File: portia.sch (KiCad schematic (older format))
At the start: 60 parts, among them J1 USB_B_Micro, J10 Conn_01x02, J11 Conn_01x02, J12 Conn_01x02, J13 Conn_01x02, J14 Conn_01x02, J15 Conn_01x02, J16 Conn_01x04, J3 Conn_01x02, J4 Conn_01x04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

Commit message: ground plane fill
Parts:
- removed D7: LED, LED_SMD:LED_0603_1608Metric, symbol Device:LED
- removed R11: R_Small, Resistor_SMD:R_0603_1608Metric, symbol Device:R_Small
- added D3: LED_ARGB, LED_SMD:LED_RGB_1210, symbol Device:LED_ARGB
- added R11, R18: 75, Resistor_SMD:R_0603_1608Metric, symbol Device:R
- added R19: 100, Resistor_SMD:R_0603_1608Metric, symbol Device:R
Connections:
- net +3V3: now also D3.1 (A)
- net 3.3V: now also U2.5 (VCC); no longer U2.2 (GND)
- net GND: now also U2.2 (GND); no longer U2.5 (VCC)
- net at U4.14 (IO12): now also R11.1
- net at U4.16 (IO13): now also R18.1
- net at U4.26 (IO4): now also R19.1
- new net: D3.2 (RK), R19.2
- new net: D3.3 (GK), R18.2
- new net: D3.4 (BK), R11.2
- no-connect marks 20 -> 25
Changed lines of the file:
@@
-	1    0    0    -1
-$EndComp
-$Comp
-L Connector:USB_B_Micro J1
-U 1 1 5C241362
-P 3450 8650
-F 0 "J1" H 3505 9117 50  0000 C CNN
-F 1 "USB_B_Micro" H 3505 9026 50  0000 C CNN
-F 2 "Connector_USB:USB_Micro-B_Amphenol_10103594-0001LF_Horizontal" H 3600 8600 50  0001 C CNN
-F 3 "~" H 3600 8600 50  0001 C CNN
-	1    3450 8650
 	1    0    0    -1
 $EndComp
@@
 Wire Wire Line
 	3750 8750 4050 8750
-Wire Wire Line
-	3750 8550 3750 8450
-Wire Wire Line
-	3800 9050 3800 9250
-Wire Wire Line
-	3450 9050 3800 9050
 $Comp
 L power:GND #PWR0112
 U 1 1 5C384A73
-P 3800 9250
-F 0 "#PWR0112" H 3800 9000 50  0001 C CNN
-F 1 "GND" H 3805 9077 50  0000 C CNN
-F 2 "" H 3800 9250 50  0001 C CNN
-F 3 "" H 3800 9250 50  0001 C CNN
-	1    3800 9250
+P 3450 9250
+F 0 "#PWR0112" H 3450 9000 50  0001 C CNN
+F 1 "GND" H 3455 9077 50  0000 C CNN
+F 2 "" H 3450 9250 50  0001 C CNN
+F 3 "" H 3450 9250 50  0001 C CNN
+	1    3450 9250
 	1    0    0    -1
 $EndComp
@@
 Wire Wire Line
 	4250 9300 4850 9300
-Wire Wire Line
-	3750 8450 3750 8100
 $Comp
 L power:+5V #PWR0115
@@
 Wire Wire Line
 	3750 8550 3900 8550
-Connection ~ 3750 8450
 Wire Wire Line
 	4100 8550 4500 8550
@@
 Wire Wire Line
 	11000 6250 11200 6250
-Wire Wire Line
-	11200 6250 11200 6700
-$Comp
-L Device:R_Small R11
-U 1 1 5C805139
-P 12300 6700
-F 0 "R11" V 12104 6700 50  0000 C CNN
-F 1 "R_Small" V 12195 6700 50  0000 C CNN
-F 2 "Resistor_SMD:R_0603_1608Metric" H 12300 6700 50  0001 C CNN
-F 3 "~" H 12300 6700 50  0001 C CNN
-	1    12300 6700
-	0    1    1    0
-$EndComp
-Wire Wire Line
-	11200 6700 12200 6700
-Wire Wire Line
-	12400 6700 12650 6700
-$Comp
-L Device:LED D7
-U 1 1 5C853C14
-P 12800 6700
-F 0 "D7" H 12792 6445 50  0000 C CNN
-F 1 "LED" H 12792 6536 50  0000 C CNN
-F 2 "LED_SMD:LED_0603_1608Metric" H 12800 6700 50  0001 C CNN
-F 3 "~" H 12800 6700 50  0001 C CNN
-	1    12800 6700
-	-1   0    0    1
-$EndComp
-Wire Wire Line
-	12950 6700 13200 6700
-$Comp
-L power:GND #PWR0135
-U 1 1 5C8D8953
-P 13200 6700
-F 0 "#PWR0135" H 13200 6450 50  0001 C CNN
-F 1 "GND" V 13205 6572 50  0000 R CNN
-F 2 "" H 13200 6700 50  0001 C CNN
-F 3 "" H 13200 6700 50  0001 C CNN
-	1    13200 6700
-	0    -1   -1   0
-$EndComp
 NoConn ~ 10050 6950
 Text Label 7250 8250 0    50   ~ 0
@@
 Wire Wire Line
 	12300 8650 13500 8650
-Wire Wire Line
-	14700 8250 14800 8250
-Wire Wire Line
-	14700 8650 14850 8650
 $Comp
 L SparkFun-Aesthetics:3.3V #SUPPLY0101
 U 1 1 5C35ADBC
-P 15350 8250
-F 0 "#SUPPLY0101" H 15350 8250 50  0001 L BNN
-F 1 "3.3V" V 15350 8379 50  0000 L CNN
-F 2 "" H 15350 8250 50  0001 C CNN
-F 3 "" H 15350 8250 50  0001 C CNN
-	1    15350 8250
-	0    1    1    0
-$EndComp
-$Comp
-L power:GND #PWR0119
-U 1 1 5C363419
-P 15000 8650
-F 0 "#PWR0119" H 15000 8400 50  0001 C CNN
-F 1 "GND" H 15005 8477 50  0000 C CNN
-F 2 "" H 15000 8650 50  0001 C CNN
-F 3 "" H 15000 8650 50  0001 C CNN
-	1    15000 8650
-	1    0    0    -1
+P 15150 9300
+F 0 "#SUPPLY0101" H 15150 9300 50  0001 L BNN
+F 1 "3.3V" V 15150 9429 50  0000 L CNN
+F 2 "" H 15150 9300 50  0001 C CNN
+F 3 "" H 15150 9300 50  0001 C CNN
+	1    15150 9300
+	0    1    1    0
 $EndComp
 $Comp
@@
 Wire Wire Line
 	13500 7700 13650 7700
-Wire Wire Line
-	14800 7700 14800 8250
 Connection ~ 13650 7700
-Wire Wire Line
-	13650 7700 14800 7700
-Connection ~ 14800 8250
-Wire Wire Line
-	14800 8250 15150 8250
 NoConn ~ 13800 8250
 NoConn ~ 13800 8350
@@
 	13350 9200 13350 8750
 Wire Wire Line
-	14650 9100 14850 9100
-Wire Wire Line
-	14850 9100 14850 8650
-Connection ~ 14850 8650
-Wire Wire Line
-	14850 8650 15000 8650
-Wire Wire Line
 	14650 9300 14800 9300
-Wire Wire Line
-	15150 9300 15150 8250
-Connection ~ 15150 8250
-Wire Wire Line
-	15150 8250 15350 8250
 $Comp
 L Device:R_Small R12
@@
 	1    0    0    -1
 $EndComp
+$Comp
+L Device:LED_ARGB D3
+U 1 1 5C32D160
+P 7950 7350
+F 0 "D3" H 7950 6883 50  0000 C CNN
+F 1 "LED_ARGB" H 7950 6974 50  0000 C CNN
+F 2 "LED_SMD:LED_RGB_1210" H 7950 7300 50  0001 C CNN
+F 3 "~" H 7950 7300 50  0001 C CNN
+	1    7950 7350
+	-1   0    0    1
+$EndComp
+$Comp
+L Device:R R11
+U 1 1 5C36CFF3
+P 8500 7150
+F 0 "R11" V 8400 7050 50  0000 C CNN
+F 1 "75" V 8400 7250 50  0000 C CNN
+F 2 "Resistor_SMD:R_0603_1608Metric" V 8430 7150 50  0001 C CNN
+F 3 "~" H 8500 7150 50  0001 C CNN
+	1    8500 7150
+	0    1    1    0
+$EndComp
+$Comp
+L Device:R R18
+U 1 1 5C36EBA1
+P 8500 7350
+F 0 "R18" V 8400 7250 50  0000 C CNN
+F 1 "75" V 8400 7450 50  0000 C CNN
+F 2 "Resistor_SMD:R_0603_1608Metric" V 8430 7350 50  0001 C CNN
+F 3 "~" H 8500 7350 50  0001 C CNN
+	1    8500 7350
+	0    1    1    0
+$EndComp
+$Comp
+L Device:R R19
+U 1 1 5C36EF8A
+P 8500 7550
+F 0 "R19" V 8400 7450 50  0000 C CNN
+F 1 "100" V 8400 7650 50  0000 C CNN
+F 2 "Resistor_SMD:R_0603_1608Metric" V 8430 7550 50  0001 C CNN
+F 3 "~" H 8500 7550 50  0001 C CNN
+	1    8500 7550
+	0    1    1    0
+$EndComp
+Wire Wire Line
+	9150 6500 8650 6500
+Wire Wire Line
+	8650 6500 8650 7150
+Wire Wire Line
+	8650 7350 9750 7350
+Wire Wire Line
+	9750 7350 9750 6950
+Wire Wire Line
+	11200 6250 11200 6950
+Wire Wire Line
+	10750 6950 10750 7550
+Wire Wire Line
+	10750 7550 8650 7550
+Wire Wire Line
+	11200 6950 10750 6950
+Wire Wire Line
+	8150 7150 8350 7150
+Wire Wire Line
+	8150 7350 8350 7350
+Wire Wire Line
+	8150 7550 8350 7550
+Wire Wire Line
+	7750 7350 7300 7350
+$Comp
+L power:+3.3V #PWR0120
+U 1 1 5C44597A
+P 7300 7350
+F 0 "#PWR0120" H 7300 7200 50  0001 C CNN
+F 1 "+3.3V" V 7315 7478 50  0000 L CNN
+F 2 "" H 7300 7350 50  0001 C CNN
+F 3 "" H 7300 7350 50  0001 C CNN
+	1    7300 7350
+	0    -1   -1   0
+$EndComp
+$Comp
+L power:GND #PWR0119
+U 1 1 5C3312B5
+P 14800 9100
+F 0 "#PWR0119" H 14800 8850 50  0001 C CNN
+F 1 "GND" V 14805 8972 50  0000 R CNN
+F 2 "" H 14800 9100 50  0001 C CNN
+F 3 "" H 14800 9100 50  0001 C CNN
+	1    14800 9100
+	0    -1   -1   0
+$EndComp
+$Comp
+L power:GND #PWR0121
+U 1 1 5C375D80
+P 14800 8250
+F 0 "#PWR0121" H 14800 8000 50  0001 C CNN
+F 1 "GND" H 14805 8077 50  0000 C CNN
+F 2 "" H 14800 8250 50  0001 C CNN
+F 3 "" H 14800 8250 50  0001 C CNN
+	1    14800 8250
+	1    0    0    -1
+$EndComp
+Wire Wire Line
+	14700 8650 15100 8650
+$Comp
+L SparkFun-Aesthetics:3.3V #SUPPLY0102
+U 1 1 5C39E3C3
+P 15150 8650
+F 0 "#SUPPLY0102" H 15150 8650 50  0001 L BNN
+F 1 "3.3V" V 15150 8779 50  0000 L CNN
+F 2 "" H 15150 8650 50  0001 C CNN
+F 3 "" H 15150 8650 50  0001 C CNN
+	1    15150 8650
+	0    1    1    0
+$EndComp
+Wire Wire Line
+	14650 9100 14800 9100
+Wire Wire Line
+	15100 7700 15100 8650
+Wire Wire Line
+	13650 7700 15100 7700
+Connection ~ 15100 8650
+Wire Wire Line
+	15100 8650 15150 8650
+NoConn ~ 13850 9100
+NoConn ~ 12300 8950
+NoConn ~ 12300 9050
+NoConn ~ 12300 9150
+NoConn ~ 12300 9250
+Wire Wire Line
+	3750 8450 3750 8100
+Wire Wire Line
+	3750 8550 3750 8450
+Connection ~ 3750 8450
+$Comp
+L Connector:USB_B_Micro J1
+U 1 1 5C241362
+P 3450 8650
+F 0 "J1" H 3505 9117 50  0000 C CNN
+F 1 "USB_B_Micro" H 3505 9026 50  0000 C CNN
+F 2 "Connector_USB:USB_Micro-B_Amphenol_10103594-0001LF_Horizontal" H 3600 8600 50  0001 C CNN
+F 3 "~" H 3600 8600 50  0001 C CNN
+	1    3450 8650
+	1    0    0    -1
+$EndComp
+Wire Wire Line
+	3450 9050 3450 9250
+Wire Wire Line
+	14700 8250 14800 8250
 $EndSCHEMATC

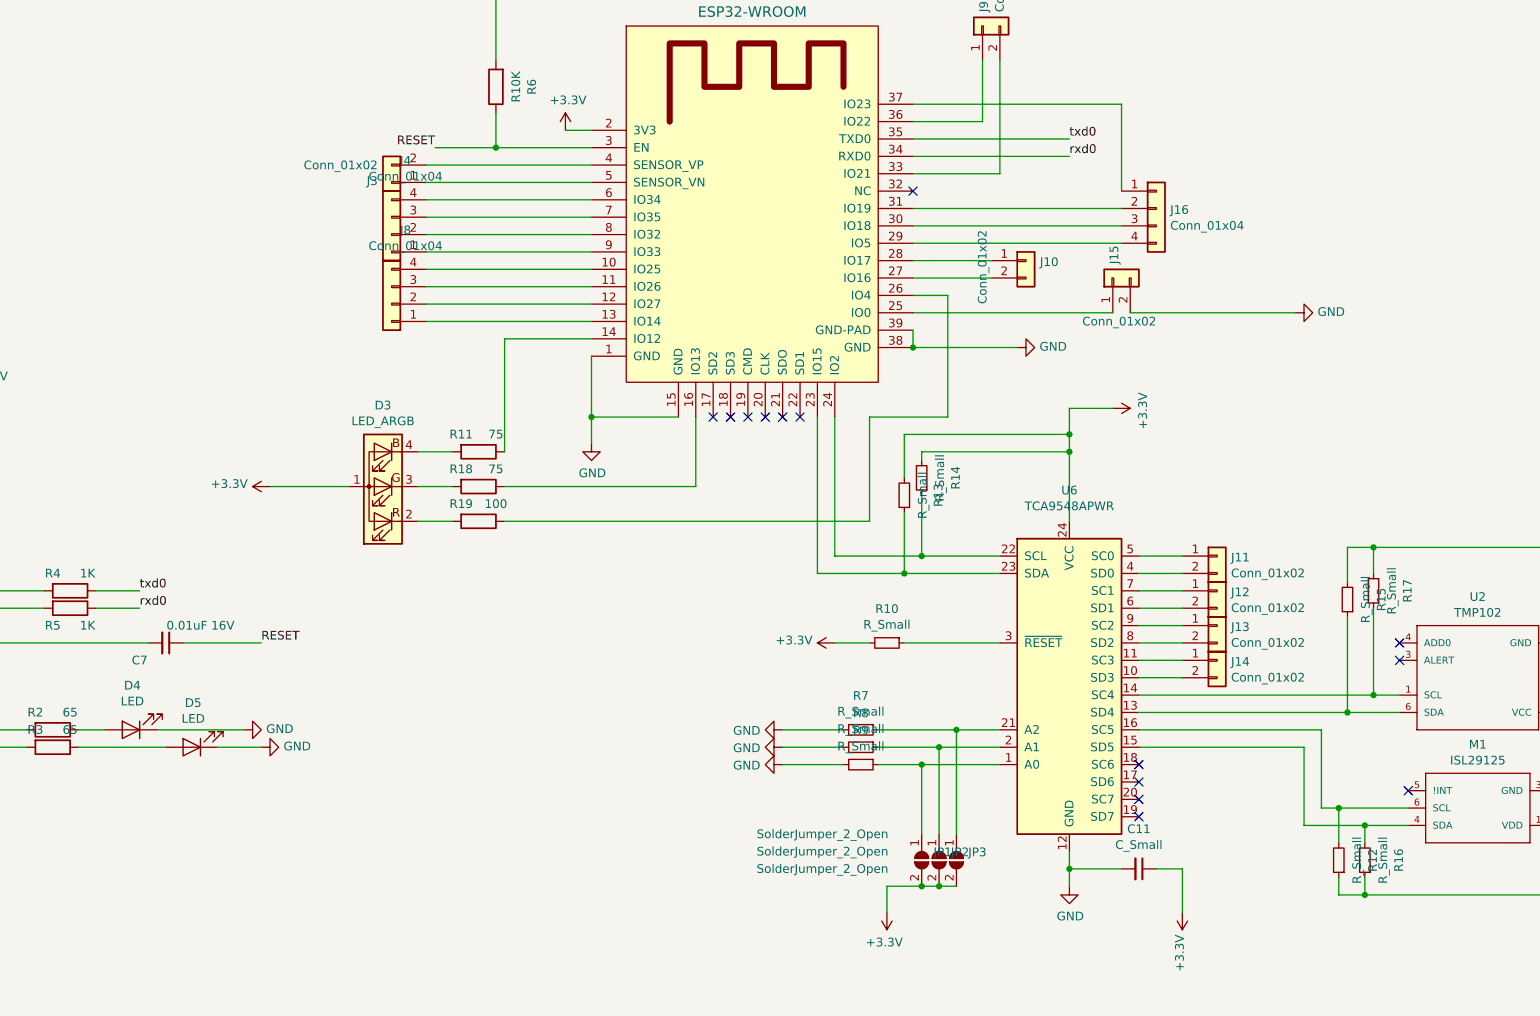
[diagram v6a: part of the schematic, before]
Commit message: added ground ports
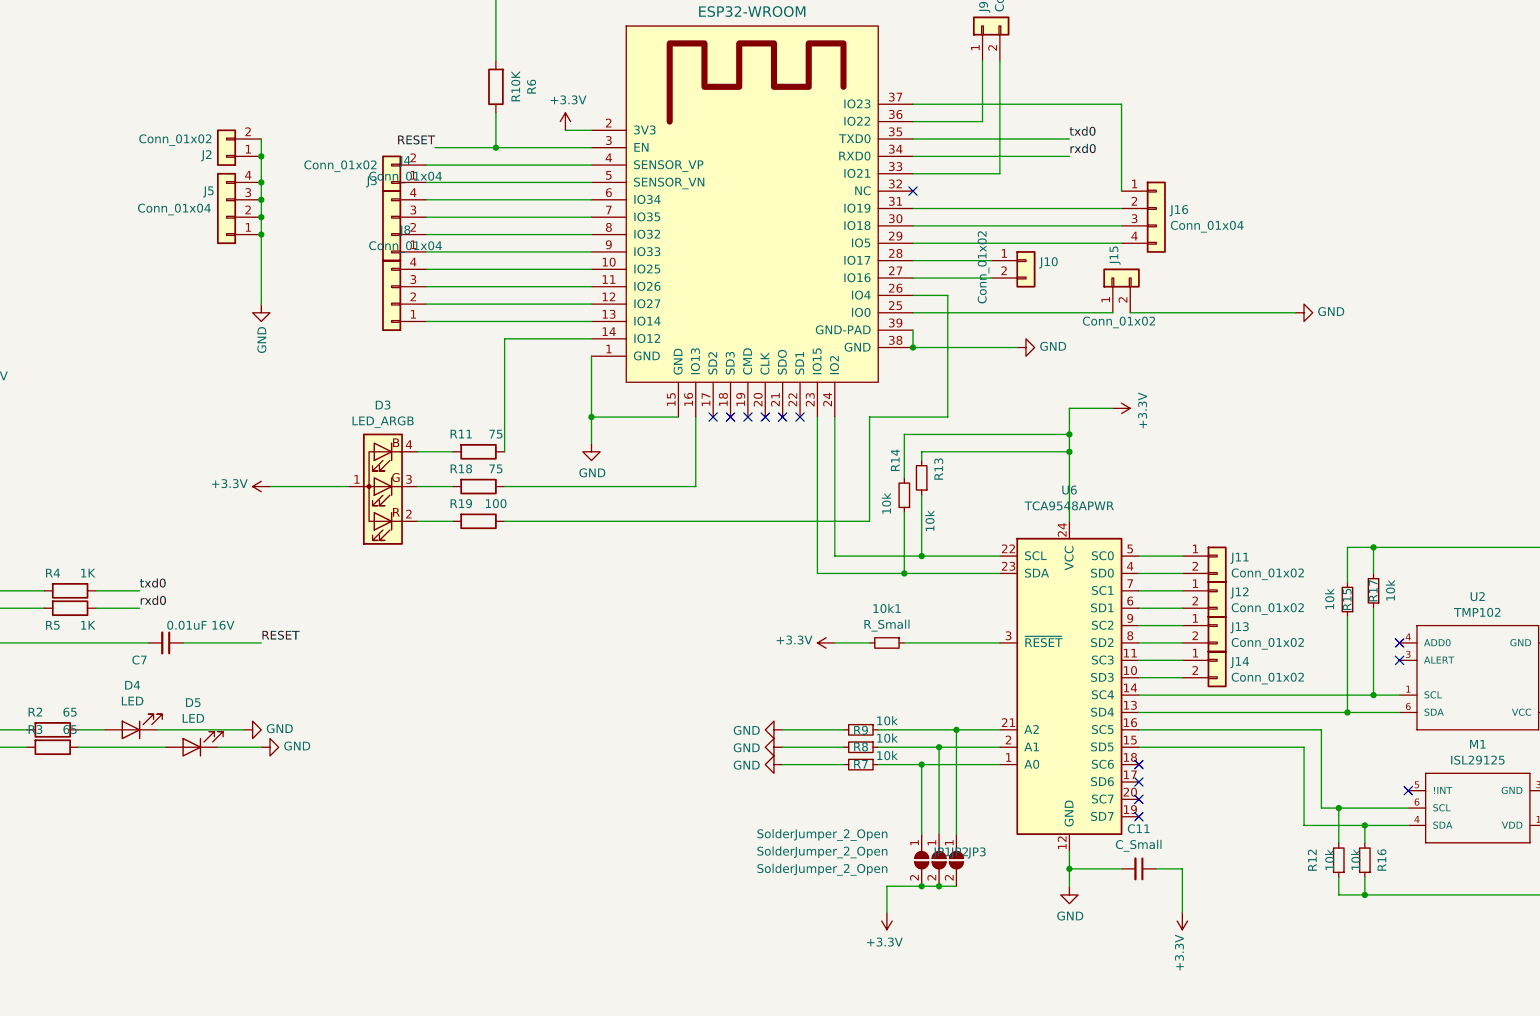
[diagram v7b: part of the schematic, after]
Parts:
- added J2: Conn_01x02, Connector_PinHeader_2.54mm:PinHeader_1x02_P2.54mm_Vertical, symbol Connector_Generic:Conn_01x02
- added J5: Conn_01x04, Connector_PinHeader_2.54mm:PinHeader_1x04_P2.54mm_Vertical, symbol Connector_Generic:Conn_01x04
- R12, R13, R14, R15, R16, R17, R7, R8, R9: value R_Small -> 10k
- renumbered R10 to 10k1
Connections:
- net GND: now also J2.1 (Pin_1), J2.2 (Pin_2), J5.1 (Pin_1), J5.2 (Pin_2), J5.3 (Pin_3), J5.4 (Pin_4)
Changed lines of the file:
@@
 	11000 6450 11000 6550
 Connection ~ 11000 6550
-$Comp
-L Interface_Expansion:TCA9548APWR U6
-U 1 1 5C3CC0F4
-P 11900 8450
-F 0 "U6" H 11900 9528 50  0000 C CNN
-F 1 "TCA9548APWR" H 11900 9437 50  0000 C CNN
-F 2 "Package_SO:TSSOP-24_4.4x7.8mm_P0.65mm" H 11900 7450 50  0001 C CNN
-F 3 "http://www.ti.com/lit/ds/symlink/tca9548a.pdf" H 11950 8700 50  0001 C CNN
-	1    11900 8450
-	1    0    0    -1
-$EndComp
 Wire Wire Line
 	11500 8750 11250 8750
@@
 P 10700 8950
 F 0 "R9" V 10504 8950 50  0000 C CNN
-F 1 "R_Small" V 10595 8950 50  0000 C CNN
+F 1 "10k" V 10650 9100 50  0000 C CNN
 F 2 "Resistor_SMD:R_0603_1608Metric" H 10700 8950 50  0001 C CNN
 F 3 "~" H 10700 8950 50  0001 C CNN
@@
 U 1 1 5C410272
 P 10700 8850
-F 0 "R8" V 10504 8850 50  0000 C CNN
-F 1 "R_Small" V 10595 8850 50  0000 C CNN
+F 0 "R8" V 10700 8850 50  0000 C CNN
+F 1 "10k" V 10650 9000 50  0000 C CNN
 F 2 "Resistor_SMD:R_0603_1608Metric" H 10700 8850 50  0001 C CNN
 F 3 "~" H 10700 8850 50  0001 C CNN
@@
 U 1 1 5C4106A4
 P 10700 8750
-F 0 "R7" V 10504 8750 50  0000 C CNN
-F 1 "R_Small" V 10595 8750 50  0000 C CNN
+F 0 "R7" V 10900 8750 50  0000 C CNN
+F 1 "10k" V 10650 8900 50  0000 C CNN
 F 2 "Resistor_SMD:R_0603_1608Metric" H 10700 8750 50  0001 C CNN
 F 3 "~" H 10700 8750 50  0001 C CNN
@@
 Wire Wire Line
 	10600 8750 10250 8750
-Wire Wire Line
-	10600 8850 10250 8850
 Wire Wire Line
 	10600 8950 10250 8950
@@
 	11500 8250 10950 8250
 $Comp
-L Device:R_Small R10
+L Device:R_Small 10k1
 U 1 1 5C494703
 P 10850 8250
-F 0 "R10" V 10654 8250 50  0000 C CNN
+F 0 "10k1" V 10654 8250 50  0000 C CNN
 F 1 "R_Small" V 10745 8250 50  0000 C CNN
 F 2 "Resistor_SMD:R_0603_1608Metric" H 10850 8250 50  0001 C CNN
@@
 U 1 1 5C3AE1A2
 P 11050 7300
-F 0 "R14" V 10854 7300 50  0000 C CNN
-F 1 "R_Small" V 10945 7300 50  0000 C CNN
+F 0 "R14" V 11200 7200 50  0000 C CNN
+F 1 "10k" V 11000 7550 50  0000 C CNN
 F 2 "Resistor_SMD:R_0603_1608Metric" H 11050 7300 50  0001 C CNN
 F 3 "~" H 11050 7300 50  0001 C CNN
@@
 U 1 1 5C3C22DB
 P 10950 7400
-F 0 "R13" V 10754 7400 50  0000 C CNN
-F 1 "R_Small" V 10845 7400 50  0000 C CNN
+F 0 "R13" V 10750 7250 50  0000 C CNN
+F 1 "10k" V 11050 7450 50  0000 C CNN
 F 2 "Resistor_SMD:R_0603_1608Metric" H 10950 7400 50  0001 C CNN
 F 3 "~" H 10950 7400 50  0001 C CNN
@@
 U 1 1 5C37A860
 P 13650 7950
-F 0 "R17" V 13454 7950 50  0000 C CNN
-F 1 "R_Small" V 13545 7950 50  0000 C CNN
+F 0 "R17" V 13650 7950 50  0000 C CNN
+F 1 "10k" V 13550 7950 50  0000 C CNN
 F 2 "Resistor_SMD:R_0603_1608Metric" H 13650 7950 50  0001 C CNN
 F 3 "~" H 13650 7950 50  0001 C CNN
@@
 U 1 1 5C382EF7
 P 13500 8000
-F 0 "R15" V 13304 8000 50  0000 C CNN
-F 1 "R_Small" V 13395 8000 50  0000 C CNN
+F 0 "R15" V 13500 8000 50  0000 C CNN
+F 1 "10k" V 13600 8000 50  0000 C CNN
 F 2 "Resistor_SMD:R_0603_1608Metric" H 13500 8000 50  0001 C CNN
 F 3 "~" H 13500 8000 50  0001 C CNN
@@
 U 1 1 5C46E7CC
 P 13450 9500
-F 0 "R12" V 13254 9500 50  0000 C CNN
-F 1 "R_Small" V 13345 9500 50  0000 C CNN
+F 0 "R12" V 13600 9500 50  0000 C CNN
+F 1 "10k" V 13500 9500 50  0000 C CNN
 F 2 "Resistor_SMD:R_0603_1608Metric" H 13450 9500 50  0001 C CNN
 F 3 "~" H 13450 9500 50  0001 C CNN
@@
 U 1 1 5C46EC48
 P 13600 9500
-F 0 "R16" V 13404 9500 50  0000 C CNN
-F 1 "R_Small" V 13495 9500 50  0000 C CNN
+F 0 "R16" V 13500 9500 50  0000 C CNN
+F 1 "10k" V 13650 9500 50  0000 C CNN
 F 2 "Resistor_SMD:R_0603_1608Metric" H 13600 9500 50  0001 C CNN
 F 3 "~" H 13600 9500 50  0001 C CNN
@@
 	15100 8650 15150 8650
 NoConn ~ 13850 9100
-NoConn ~ 12300 8950
-NoConn ~ 12300 9050
-NoConn ~ 12300 9150
-NoConn ~ 12300 9250
 Wire Wire Line
 	3750 8450 3750 8100
@@
 Wire Wire Line
 	14700 8250 14800 8250
+$Comp
+L Interface_Expansion:TCA9548APWR U6
+U 1 1 5C3CC0F4
+P 11900 8450
+F 0 "U6" H 11900 9528 50  0000 C CNN
+F 1 "TCA9548APWR" H 11900 9437 50  0000 C CNN
+F 2 "Package_SO:TSSOP-24_4.4x7.8mm_P0.65mm" H 11900 7450 50  0001 C CNN
+F 3 "http://www.ti.com/lit/ds/symlink/tca9548a.pdf" H 11950 8700 50  0001 C CNN
+	1    11900 8450
+	1    0    0    -1
+$EndComp
+Wire Wire Line
+	10600 8850 10250 8850
+NoConn ~ 12300 8950
+NoConn ~ 12300 9050
+NoConn ~ 12300 9150
+NoConn ~ 12300 9250
+$Comp
+L Connector_Generic:Conn_01x04 J5
+U 1 1 5C3EA5E6
+P 7050 5800
+F 0 "J5" H 7150 5650 50  0000 C CNN
+F 1 "Conn_01x04" H 7350 5750 50  0000 C CNN
+F 2 "Connector_PinHeader_2.54mm:PinHeader_1x04_P2.54mm_Vertical" H 7050 5800 50  0001 C CNN
+F 3 "~" H 7050 5800 50  0001 C CNN
+	1    7050 5800
+	-1   0    0    1
+$EndComp
+$Comp
+L Connector_Generic:Conn_01x02 J2
+U 1 1 5C3EB369
+P 7050 5450
+F 0 "J2" H 7130 5442 50  0000 L CNN
+F 1 "Conn_01x02" H 7130 5351 50  0000 L CNN
+F 2 "Connector_PinHeader_2.54mm:PinHeader_1x02_P2.54mm_Vertical" H 7050 5450 50  0001 C CNN
+F 3 "~" H 7050 5450 50  0001 C CNN
+	1    7050 5450
+	-1   0    0    1
+$EndComp
+Wire Wire Line
+	7250 5350 7250 5450
+Connection ~ 7250 5450
+Wire Wire Line
+	7250 5450 7250 5600
+Connection ~ 7250 5600
+Wire Wire Line
+	7250 5600 7250 5700
+Connection ~ 7250 5700
+Wire Wire Line
+	7250 5700 7250 5800
+Connection ~ 7250 5800
+Wire Wire Line
+	7250 5800 7250 5900
+Connection ~ 7250 5900
+Wire Wire Line
+	7250 5900 7250 6300
+$Comp
+L power:GND #PWR0130
+U 1 1 5C40034F
+P 7250 6300
+F 0 "#PWR0130" H 7250 6050 50  0001 C CNN
+F 1 "GND" V 7255 6172 50  0000 R CNN
+F 2 "" H 7250 6300 50  0001 C CNN
+F 3 "" H 7250 6300 50  0001 C CNN
+	1    7250 6300
+	1    0    0    -1
+$EndComp
 $EndSCHEMATC
